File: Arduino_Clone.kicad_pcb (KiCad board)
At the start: 2 copper layers, 20 parts, among them J1 Digital Pins, J2 Serial, J3 ICSP, J4 I2C, J5 Analog Pins, SW1 SW_SPST, U1 24LC1025, U2 24LC1025, U3 DS1337+, U4 ATMEGA328P-AU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

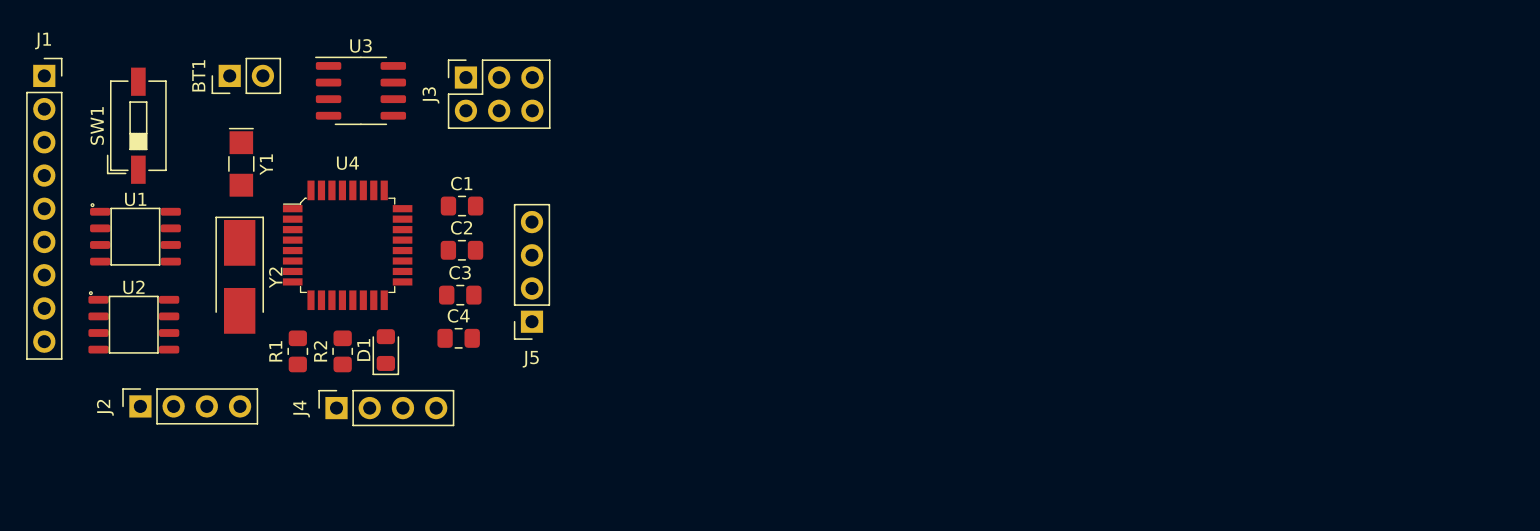
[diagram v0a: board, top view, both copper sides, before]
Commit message: Second version of component placement on pcb layout.
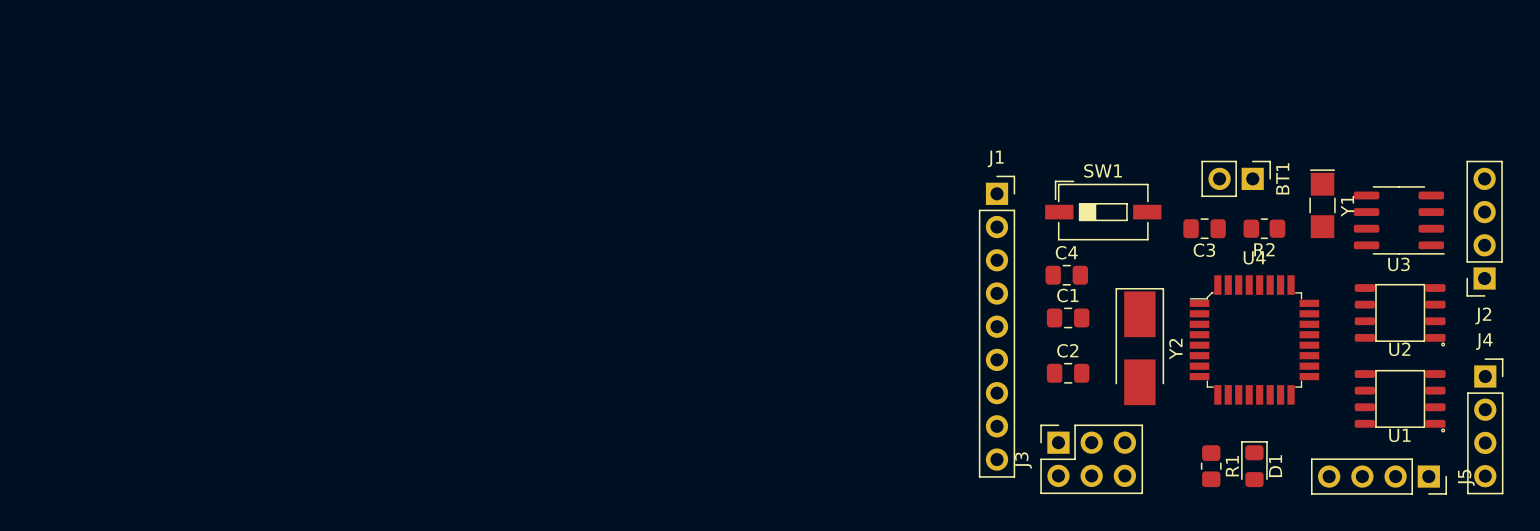
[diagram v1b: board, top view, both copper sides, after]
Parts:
- moved J2 103.3 mm to (138.3, 81.8), turned to 180 degrees
- moved U1 97.6 mm to (131.8, 91.0), turned to 180 degrees
- moved U2 96.9 mm to (131.8, 84.4), turned to 180 degrees
- moved J4 87.9 mm to (138.3, 89.3), turned to 0 degrees
- moved Y1 82.7 mm to (125.9, 76.2)
- moved U3 80.0 mm to (131.7, 77.3), turned to 180 degrees
- moved BT1 78.6 mm to (120.5, 74.2), turned to 270 degrees
- moved SW1 74.1 mm to (109.1, 76.7), turned to 0 degrees
- moved J1 73.4 mm to (101.0, 75.3)
- moved R2 71.1 mm to (121.4, 78.0), turned to 180 degrees
- moved R1 70.4 mm to (117.3, 96.1), turned to 270 degrees
- moved U4 69.7 mm to (120.7, 86.5)
- moved J5 69.6 mm to (134.0, 96.9), turned to 270 degrees
- moved Y2 69.1 mm to (111.9, 87.1)
- moved D1 67.0 mm to (120.7, 96.1), turned to 270 degrees
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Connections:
- J4 pad 4: /SCK -> /SCL
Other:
- copper layers 2 -> 4

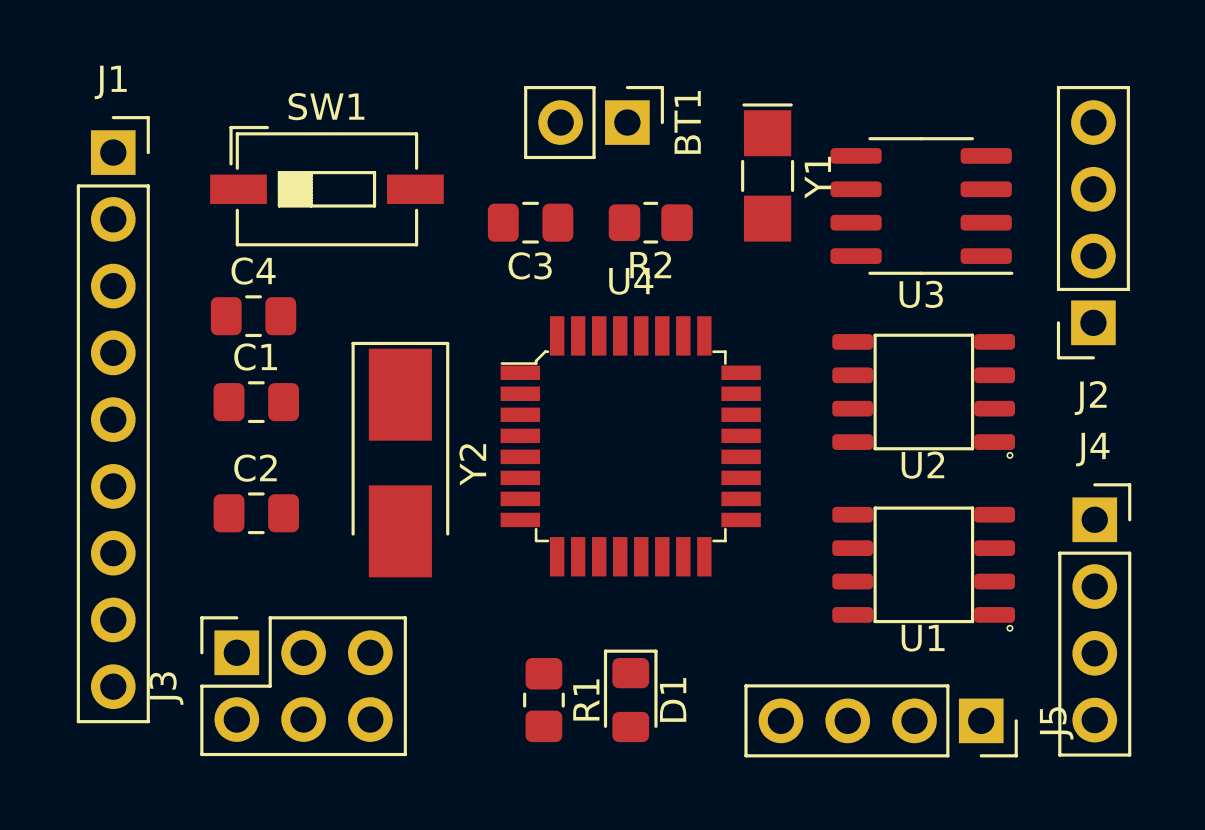
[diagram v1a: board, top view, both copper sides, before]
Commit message: Finished PCB Layout.
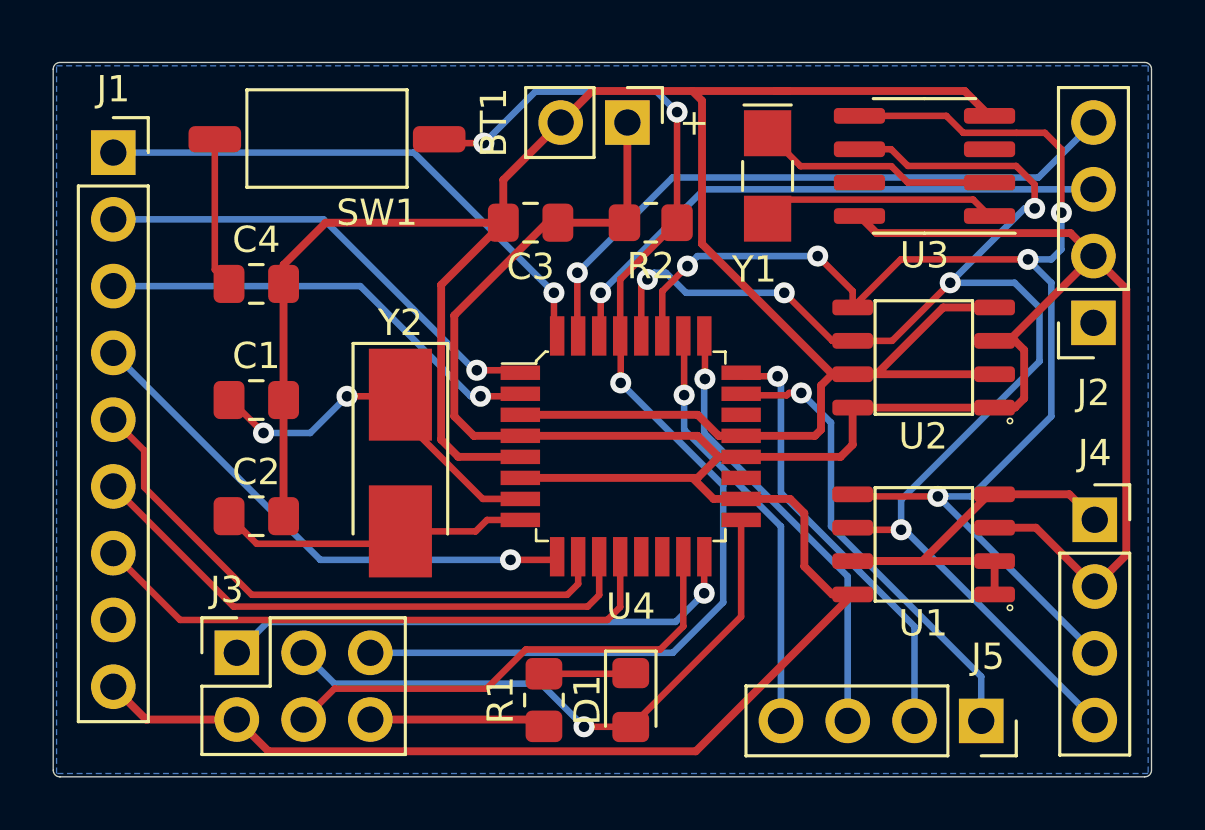
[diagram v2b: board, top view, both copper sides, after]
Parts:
- added G***: LOGO, Footprints:Zelda_Triforce, B.Cu at (109.2, 78.2)
- SW1: footprint Button_Switch_SMD:SW_DIP_SPSTx01_Slide_6.7x4.1mm_W6.73mm_P2.54mm_LowProfile_JPin -> Footprints:SPST_SW
- moved SW1 1.91 mm to (109.1, 74.8)
- moved U3 1.53 mm to (131.8, 75.8)
- moved U2 1.31 mm to (131.8, 83.1)
- moved C4 1.23 mm to (106.4, 80.3)
- moved U1 0.78 mm to (131.8, 90.2)
- moved C2 0.11 mm to (106.4, 89.1)
- moved C1 0.08 mm to (106.4, 84.7)
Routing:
- net /Vcc: track 0.00 -> 124.4 mm
- net GND: track 0.00 -> 117.2 mm
- net /SDA: track 0.00 -> 55.3 mm, vias 0 -> 5
- net /SCL: track 0.00 -> 55.2 mm, vias 0 -> 5
- net /RESET: track 0.00 -> 45.6 mm, vias 0 -> 3
- net /TX: track 0.00 -> 24.4 mm, vias 0 -> 1
- net /SCK: track 0.00 -> 23.2 mm, vias 0 -> 1
- net /D6: track 0.00 -> 22.5 mm
- net /D8: track 0.00 -> 22.5 mm
- net /RX: track 0.00 -> 22.0 mm, vias 0 -> 1
- net /D7: track 0.00 -> 22.0 mm
- net /D2: track 0.00 -> 20.7 mm, vias 0 -> 1
- net /D5: track 0.00 -> 20.2 mm, vias 0 -> 1
- net /MISO: track 0.00 -> 20.1 mm, vias 0 -> 1
- net /MOSI: track 0.00 -> 18.6 mm
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- added copper zone on B.Cu, net GND
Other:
- board outline added: 41.8 x 27.2 mm
- copper layers 4 -> 2
- board text added: "+"
- board text added: "Arduino Clone V 1.0 Made By: Brycen Dhom Feb. 6 2021"
